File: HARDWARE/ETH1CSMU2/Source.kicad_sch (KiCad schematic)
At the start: 99 parts, among them Q901 FDV301N, U901 DAC8565ICPW, U902 AD9834BRUZ, U903 MC74AC161DR2G, U904 MAX6102EUR, U905 MAX5217GUA+, U906 SN74AHC1G14DBVT, U907 OPA2141AID, U908 MC74AC161DR2G, U909 SN74AUP1G79DCKR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

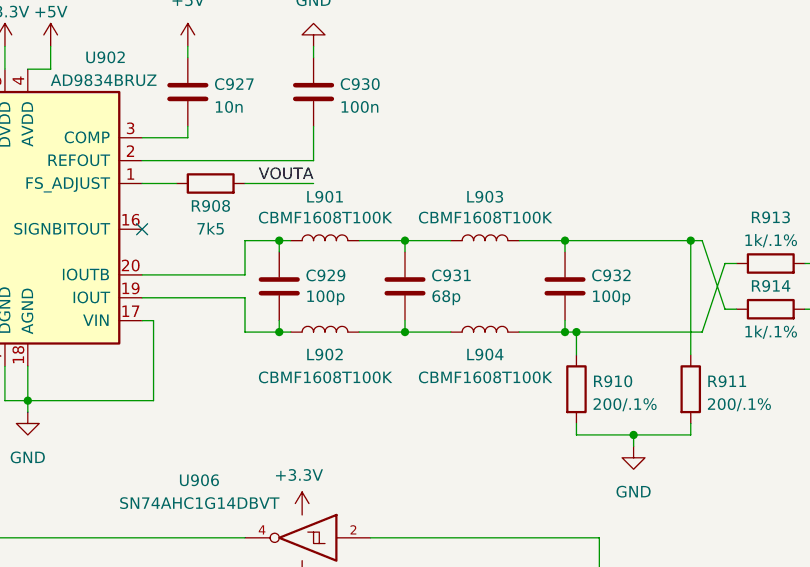
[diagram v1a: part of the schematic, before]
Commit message: Converter HW to KiCAD 7.0. Fixed 3D model paths.
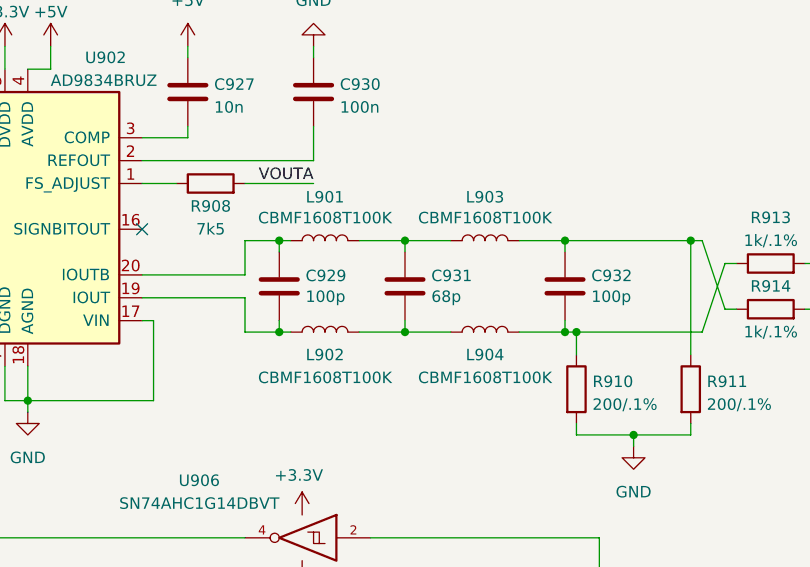
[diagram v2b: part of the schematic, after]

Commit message: Software development
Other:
- note added: "-25mV - +25mV"
- note added: "0 - 2V5"
- note added: "2V5"
- moved on the sheet: U904
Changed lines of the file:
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@@
   (junction (at 133.35 262.89) (diameter 0) (color 0 0 0 0)
   )
+  (junction (at 182.88 31.75) (diameter 0) (color 0 0 0 0)
+  )
   (junction (at 114.3 189.23) (diameter 0) (color 0 0 0 0)
   )
@@
   (junction (at 209.55 133.35) (diameter 0) (color 0 0 0 0)
   )
-  (junction (at 182.88 31.75) (diameter 0) (color 0 0 0 0)
-  )
   (junction (at 281.94 138.43) (diameter 0) (color 0 0 0 0)
   )
@@
     (stroke (width 0) (type default))
   )
+  (wire (pts (xy 182.88 31.75) (xy 182.88 53.34))
+    (stroke (width 0) (type default))
+  )
   (wire (pts (xy 34.29 262.89) (xy 40.64 262.89))
     (stroke (width 0) (type default))
@@
     (stroke (width 0) (type default))
   )
-  (wire (pts (xy 275.59 36.83) (xy 280.67 36.83))
+  (wire (pts (xy 275.59 36.83) (xy 294.64 36.83))
     (stroke (width 0) (type default))
   )
@@
     (stroke (width 0) (type default))
   )
-  (wire (pts (xy 182.88 31.75) (xy 182.88 53.34))
-    (stroke (width 0) (type default))
-  )
   (wire (pts (xy 246.38 44.45) (xy 246.38 45.72))
     (stroke (width 0) (type default))
@@
     (stroke (width 0) (type default))
   )
-  (wire (pts (xy 176.53 31.75) (xy 182.88 31.75))
+  (wire (pts (xy 152.4 31.75) (xy 182.88 31.75))
     (stroke (width 0) (type default))
   )
@@
     (effects (font (size 1.27 1.27)) (justify left bottom))
   )
+  (text "0 - 2V5" (at 196.85 62.23 0)
+    (effects (font (size 1.27 1.27)) (justify left bottom))
+  )
   (text "OFFSET DAC" (at 125.73 16.51 0)
     (effects (font (size 1.27 1.27)) (justify left bottom))
   )
+  (text "-25mV - +25mV" (at 276.86 35.56 0)
+    (effects (font (size 1.27 1.27)) (justify left bottom))
+  )
+  (text "2V5" (at 166.37 30.48 0)
+    (effects (font (size 1.27 1.27)) (justify left bottom))
+  )
   (text "DAC" (at 13.97 16.51 0)
     (effects (font (size 1.27 1.27)) (justify left bottom))
@@
     (effects (font (size 1.27 1.27)) (justify right))
   )
-  (hierarchical_label "VOUT_OFFSET" (shape output) (at 280.67 36.83 0) (fields_autoplaced)
+  (hierarchical_label "VOUT_OFFSET" (shape output) (at 294.64 36.83 0) (fields_autoplaced)
     (effects (font (size 1.27 1.27)) (justify left))
   )
@@
     )
   )
-  (symbol (lib_id "power:GND") (at 166.37 39.37 0) (unit 1)
+  (symbol (lib_id "power:GND") (at 142.24 39.37 0) (unit 1)
     (in_bom yes) (on_board yes) (dnp no) (fields_autoplaced)
-    (property "Reference" "#PWR0931" (at 166.37 45.72 0)
+    (property "Reference" "#PWR0931" (at 142.24 45.72 0)
       (effects (font (size 1.27 1.27)) hide)
     )
-    (property "Value" "GND" (at 166.37 43.8134 0)
+    (property "Value" "GND" (at 142.24 43.8134 0)
       (effects (font (size 1.27 1.27)))
     )
-    (property "Footprint" "" (at 166.37 39.37 0)
+    (property "Footprint" "" (at 142.24 39.37 0)
       (effects (font (size 1.27 1.27)) hide)
     )
-    (property "Datasheet" "" (at 166.37 39.37 0)
+    (property "Datasheet" "" (at 142.24 39.37 0)
       (effects (font (size 1.27 1.27)) hide)
     )
@@
     )
   )
-  (symbol (lib_id "power:+5V") (at 166.37 24.13 0) (unit 1)
+  (symbol (lib_id "power:+5V") (at 142.24 24.13 0) (unit 1)
     (in_bom yes) (on_board yes) (dnp no) (fields_autoplaced)
-    (property "Reference" "#PWR0930" (at 166.37 27.94 0)
+    (property "Reference" "#PWR0930" (at 142.24 27.94 0)
       (effects (font (size 1.27 1.27)) hide)
     )
-    (property "Value" "+5V" (at 166.37 20.5542 0)
+    (property "Value" "+5V" (at 142.24 20.5542 0)
       (effects (font (size 1.27 1.27)))
     )
-    (property "Footprint" "" (at 166.37 24.13 0)
+    (property "Footprint" "" (at 142.24 24.13 0)
       (effects (font (size 1.27 1.27)) hide)
     )
-    (property "Datasheet" "" (at 166.37 24.13 0)
+    (property "Datasheet" "" (at 142.24 24.13 0)
       (effects (font (size 1.27 1.27)) hide)
     )
@@
     )
   )
-  (symbol (lib_id "Reference_Voltage:MAX6102") (at 168.91 31.75 0) (unit 1)
+  (symbol (lib_id "Reference_Voltage:MAX6102") (at 144.78 31.75 0) (unit 1)
     (in_bom yes) (on_board yes) (dnp no) (fields_autoplaced)
-    (property "Reference" "U904" (at 163.0681 30.9153 0)
+    (property "Reference" "U904" (at 138.9381 30.9153 0)
       (effects (font (size 1.27 1.27)) (justify right))
     )
-    (property "Value" "MAX6102EUR" (at 163.0681 33.4522 0)
+    (property "Value" "MAX6102EUR" (at 138.9381 33.4522 0)
       (effects (font (size 1.27 1.27)) (justify right))
     )
-    (property "Footprint" "Package_TO_SOT_SMD:SOT-23" (at 171.45 39.37 0)
+    (property "Footprint" "Package_TO_SOT_SMD:SOT-23" (at 147.32 39.37 0)
       (effects (font (size 1.27 1.27) italic) hide)
     )
-    (property "Datasheet" "http://datasheets.maximintegrated.com/en/ds/MAX6100-MAX6107.pdf" (at 171.45 40.64 0)
+    (property "Datasheet" "http://datasheets.maximintegrated.com/en/ds/MAX6100-MAX6107.pdf" (at 147.32 40.64 0)
       (effects (font (size 1.27 1.27) italic) hide)
     )

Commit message: Software development
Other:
- note added: "-12V - +12V"
- note added: "0 - 1.25V"
- moved on the sheet: C937, R931, R932, R933, R937, U913, U915

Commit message: Software development and hardware changes.
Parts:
- R901: now not fitted
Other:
- note added: "0-2.5 V"
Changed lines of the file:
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@@
     (stroke (width 0) (type default))
   )
-  (wire (pts (xy 87.63 31.75) (xy 92.71 31.75))
+  (wire (pts (xy 87.63 31.75) (xy 104.14 31.75))
     (stroke (width 0) (type default))
   )
@@
     (stroke (width 0) (type default))
   )
-  (wire (pts (xy 87.63 34.29) (xy 92.71 34.29))
+  (wire (pts (xy 87.63 34.29) (xy 104.14 34.29))
     (stroke (width 0) (type default))
   )
@@
     (stroke (width 0) (type default))
   )
-  (wire (pts (xy 87.63 39.37) (xy 92.71 39.37))
+  (wire (pts (xy 87.63 39.37) (xy 104.14 39.37))
     (stroke (width 0) (type default))
   )
@@
     (stroke (width 0) (type default))
   )
-  (wire (pts (xy 87.63 36.83) (xy 92.71 36.83))
+  (wire (pts (xy 87.63 36.83) (xy 104.14 36.83))
     (stroke (width 0) (type default))
   )
@@
   (wire (pts (xy 15.24 241.3) (xy 15.24 240.03))
     (stroke (width 0) (type default))
+  )
+  (text_box "Externeal reference must be 4V - 4.99V. The 2.5V is to small. Best solution is to use REF5040ID. DAC1_LDAC is not needed (connect to GND)."
+    (at 43.18 77.47 0) (size 58.42 7.62)
+    (stroke (width 0) (type default))
+    (fill (type none))
+    (effects (font (size 1.27 1.27)) (justify left top))
   )
   (text "0 - 1.25V" (at 337.82 181.61 0)
@@
     (effects (font (size 1.27 1.27)) (justify left bottom))
   )
+  (text "0-2.5 V" (at 92.71 29.21 0)
+    (effects (font (size 1.27 1.27)) (justify left bottom))
+  )
   (text "OFFSET DAC" (at 125.73 16.51 0)
     (effects (font (size 1.27 1.27)) (justify left bottom))
@@
     (effects (font (size 1.27 1.27)) (justify left))
   )
-  (hierarchical_label "VC_-IN" (shape output) (at 92.71 34.29 0) (fields_autoplaced)
+  (hierarchical_label "VC_-IN" (shape output) (at 104.14 34.29 0) (fields_autoplaced)
     (effects (font (size 1.27 1.27)) (justify left))
   )
@@
     (effects (font (size 1.27 1.27)) (justify right))
   )
-  (hierarchical_label "VC_SRC" (shape output) (at 92.71 39.37 0) (fields_autoplaced)
+  (hierarchical_label "VC_SRC" (shape output) (at 104.14 39.37 0) (fields_autoplaced)
     (effects (font (size 1.27 1.27)) (justify left))
   )
@@
     (effects (font (size 1.27 1.27)) (justify right))
   )
-  (hierarchical_label "VC_+IN" (shape output) (at 92.71 31.75 0) (fields_autoplaced)
+  (hierarchical_label "VC_+IN" (shape output) (at 104.14 31.75 0) (fields_autoplaced)
     (effects (font (size 1.27 1.27)) (justify left))
   )
@@
     (effects (font (size 1.27 1.27)) (justify right))
   )
-  (hierarchical_label "VC_SINK" (shape output) (at 92.71 36.83 0) (fields_autoplaced)
+  (hierarchical_label "VC_SINK" (shape output) (at 104.14 36.83 0) (fields_autoplaced)
     (effects (font (size 1.27 1.27)) (justify left))
   )
@@
   )
   (symbol (lib_id "Device:R") (at 22.86 66.04 0) (unit 1)
-    (in_bom yes) (on_board yes) (dnp no) (fields_autoplaced)
+    (in_bom yes) (on_board yes) (dnp yes) (fields_autoplaced)
     (property "Reference" "R901" (at 25.4 64.7699 0)
       (effects (font (size 1.27 1.27)) (justify left))

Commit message: Software development, added comments to schematic.
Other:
- note added: "gain 3x"
- moved on the sheet: C921, C927, C929, C930, C931, C932, C933, C934, C935, C937, C938, L901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

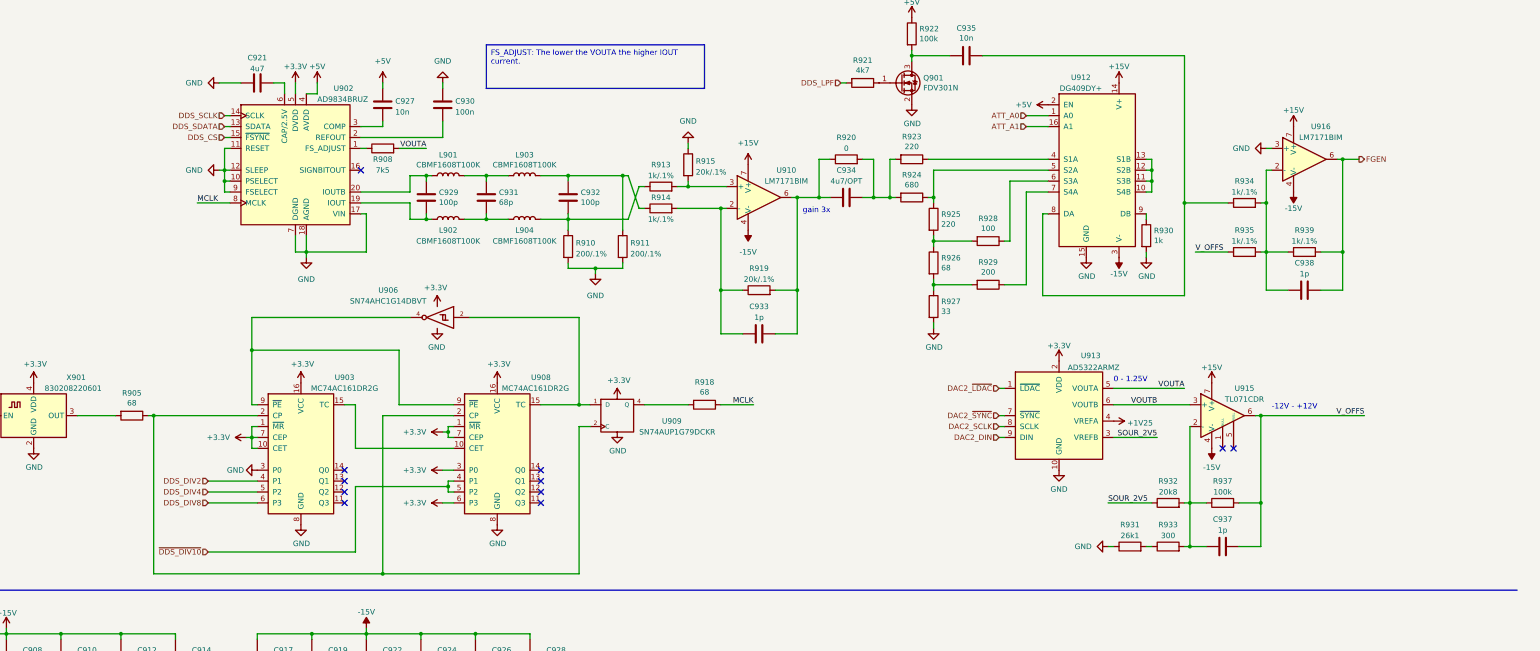
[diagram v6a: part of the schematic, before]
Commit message: Software development and hardware changes. FGEN code works.
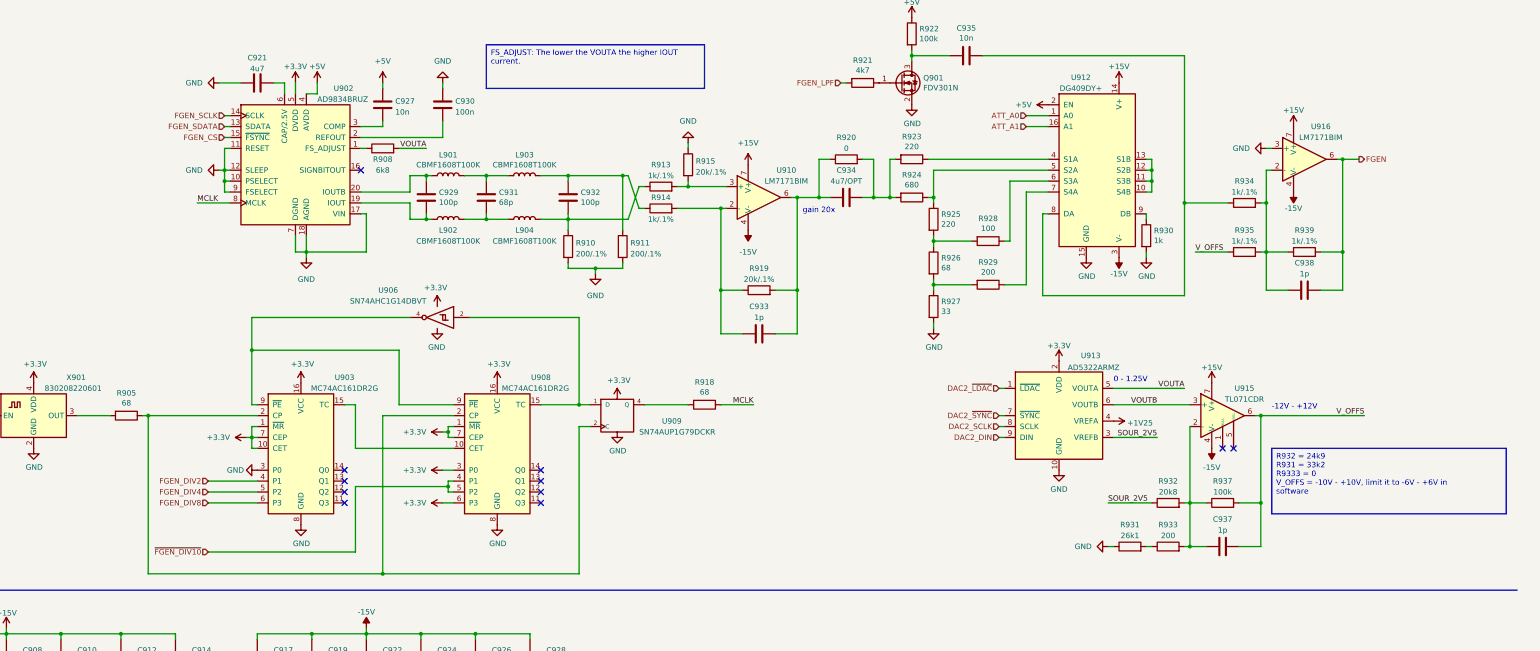
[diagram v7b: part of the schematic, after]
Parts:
- R908: value 7k5 -> 6k8
- R933: value 300 -> 200
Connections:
- net DDS_CS renamed FGEN_CS
- net DDS_DIV2 renamed FGEN_DIV2
- net DDS_DIV4 renamed FGEN_DIV4
- net DDS_DIV8 renamed FGEN_DIV8
- net DDS_LPF renamed FGEN_LPF
- net DDS_SCLK renamed FGEN_SCLK
- net DDS_SDATA renamed FGEN_SDATA
- net ~{DDS_DIV10} renamed ~{FGEN_DIV10}
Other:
- note added: "gain 20x"
- note removed: "gain 3x"
- moved on the sheet: R905
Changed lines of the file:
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@@
   (junction (at 182.88 31.75) (diameter 0) (color 0 0 0 0)
   )
-  (junction (at 88.9 189.23) (diameter 0) (color 0 0 0 0)
-  )
   (junction (at 35.56 44.45) (diameter 0) (color 0 0 0 0)
   )
@@
   (junction (at 260.35 138.43) (diameter 0) (color 0 0 0 0)
   )
+  (junction (at 87.63 189.23) (diameter 0) (color 0 0 0 0)
+  )
   (junction (at 111.76 173.99) (diameter 0) (color 0 0 0 0)
   )
@@
     (stroke (width 0) (type default))
   )
-  (wire (pts (xy 113.03 189.23) (xy 88.9 189.23))
+  (wire (pts (xy 87.63 189.23) (xy 113.03 189.23))
     (stroke (width 0) (type default))
   )
@@
     (stroke (width 0) (type default))
   )
-  (wire (pts (xy 88.9 226.06) (xy 88.9 189.23))
+  (wire (pts (xy 87.63 226.06) (xy 87.63 189.23))
     (stroke (width 0) (type default))
   )
@@
     (stroke (width 0) (type default))
   )
-  (wire (pts (xy 80.01 189.23) (xy 71.12 189.23))
+  (wire (pts (xy 78.74 189.23) (xy 71.12 189.23))
     (stroke (width 0) (type default))
   )
@@
     (stroke (width 0) (type default))
   )
+  (wire (pts (xy 87.63 189.23) (xy 86.36 189.23))
+    (stroke (width 0) (type default))
+  )
   (wire (pts (xy 270.51 160.02) (xy 270.51 158.75))
     (stroke (width 0) (type default))
@@
     (stroke (width 0) (type default))
   )
-  (wire (pts (xy 142.24 226.06) (xy 88.9 226.06))
+  (wire (pts (xy 142.24 226.06) (xy 87.63 226.06))
     (stroke (width 0) (type default))
   )
@@
     (stroke (width 0) (type default))
   )
-  (wire (pts (xy 88.9 189.23) (xy 87.63 189.23))
-    (stroke (width 0) (type default))
-  )
   (wire (pts (xy 297.18 129.54) (xy 269.24 129.54))
     (stroke (width 0) (type default))
@@
     (effects (font (size 1.27 1.27)) (justify left top))
   )
+  (text_box "R932 = 24k9\nR931 = 33k2\nR9333 = 0\nV_OFFS = -10V - +10V, limit it to -6V - +6V in software\n"
+    (at 349.25 196.85 0) (size 54.61 15.24)
+    (stroke (width 0) (type default))
+    (fill (type none))
+    (effects (font (size 1.27 1.27)) (justify left top))
+  )
   (text_box "FS_ADJUST: The lower the VOUTA the higher IOUT current. "
     (at 166.37 102.87 0) (size 50.8 10.16)
@@
     (effects (font (size 1.27 1.27)) (justify left bottom))
   )
-  (text "gain 3x" (at 240.03 142.24 0)
+  (text "gain 20x" (at 240.03 142.24 0)
     (effects (font (size 1.27 1.27)) (justify left bottom))
   )
@@
     (effects (font (size 1.27 1.27)) (justify right bottom))
   )
-  (hierarchical_label "DDS_DIV4" (shape input) (at 101.6 207.01 180) (fields_autoplaced)
+  (hierarchical_label "FGEN_DIV4" (shape input) (at 101.6 207.01 180) (fields_autoplaced)
     (effects (font (size 1.27 1.27)) (justify right))
   )
@@
     (effects (font (size 1.27 1.27)) (justify left))
   )
-  (hierarchical_label "DDS_DIV2" (shape input) (at 101.6 204.47 180) (fields_autoplaced)
+  (hierarchical_label "FGEN_DIV2" (shape input) (at 101.6 204.47 180) (fields_autoplaced)
     (effects (font (size 1.27 1.27)) (justify right))
   )
-  (hierarchical_label "DDS_SCLK" (shape input) (at 105.41 119.38 180) (fields_autoplaced)
+  (hierarchical_label "FGEN_SCLK" (shape input) (at 105.41 119.38 180) (fields_autoplaced)
     (effects (font (size 1.27 1.27)) (justify right))
   )
@@
     (effects (font (size 1.27 1.27)) (justify right))
   )
-  (hierarchical_label "~{DDS_DIV10}" (shape input) (at 101.6 220.98 180) (fields_autoplaced)
+  (hierarchical_label "~{FGEN_DIV10}" (shape input) (at 101.6 220.98 180) (fields_autoplaced)
     (effects (font (size 1.27 1.27)) (justify right))
   )
-  (hierarchical_label "DDS_DIV8" (shape input) (at 101.6 209.55 180) (fields_autoplaced)
+  (hierarchical_label "FGEN_DIV8" (shape input) (at 101.6 209.55 180) (fields_autoplaced)
     (effects (font (size 1.27 1.27)) (justify right))
   )
@@
     (effects (font (size 1.27 1.27)) (justify left))
   )
-  (hierarchical_label "DDS_CS" (shape input) (at 105.41 124.46 180) (fields_autoplaced)
+  (hierarchical_label "FGEN_CS" (shape input) (at 105.41 124.46 180) (fields_autoplaced)
     (effects (font (size 1.27 1.27)) (justify right))
   )
@@
     (effects (font (size 1.27 1.27)) (justify right))
   )
-  (hierarchical_label "DDS_LPF" (shape input) (at 248.92 111.76 180) (fields_autoplaced)
+  (hierarchical_label "FGEN_LPF" (shape input) (at 248.92 111.76 180) (fields_autoplaced)
     (effects (font (size 1.27 1.27)) (justify right))
   )
@@
     (effects (font (size 1.27 1.27)) (justify left))
   )
-  (hierarchical_label "DDS_SDATA" (shape input) (at 105.41 121.92 180) (fields_autoplaced)
+  (hierarchical_label "FGEN_SDATA" (shape input) (at 105.41 121.92 180) (fields_autoplaced)
     (effects (font (size 1.27 1.27)) (justify right))
   )
@@
       (effects (font (size 1.27 1.27)))
     )
-    (property "Value" "300" (at 325.12 217.17 90)
+    (property "Value" "200" (at 325.12 217.17 90)
       (effects (font (size 1.27 1.27)))
     )
@@
       (effects (font (size 1.27 1.27)))
     )
-    (property "Value" "7k5" (at 142.24 132.08 90)
+    (property "Value" "6k8" (at 142.24 132.08 90)
       (effects (font (size 1.27 1.27)))
     )
@@
     )
   )
-  (symbol (lib_id "Device:R") (at 83.82 189.23 270) (unit 1)
+  (symbol (lib_id "Device:R") (at 82.55 189.23 270) (unit 1)
     (in_bom yes) (on_board yes) (dnp no)
-    (property "Reference" "R905" (at 83.82 183.9722 90)
+    (property "Reference" "R905" (at 82.55 183.9722 90)
       (effects (font (size 1.27 1.27)))
     )
-    (property "Value" "68" (at 83.82 186.2836 90)
+    (property "Value" "68" (at 82.55 186.2836 90)
       (effects (font (size 1.27 1.27)))
     )
-    (property "Footprint" "Resistor_SMD:R_0603_1608Metric_Pad0.98x0.95mm_HandSolder" (at 83.82 187.452 90)
+    (property "Footprint" "Resistor_SMD:R_0603_1608Metric_Pad0.98x0.95mm_HandSolder" (at 82.55 187.452 90)
       (effects (font (size 1.27 1.27)) hide)
     )
-    (property "Datasheet" "~" (at 83.82 189.23 0)
+    (property "Datasheet" "~" (at 82.55 189.23 0)
       (effects (font (size 1.27 1.27)) hide)
     )

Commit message: Development
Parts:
- C934: value 4u7/OPT -> 4u7
- R920: now not fitted
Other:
- note added: "VREF"
- note added: "gain 8x"
- note removed: "0-2.5 V"
- note removed: "gain 20x"
- moved on the sheet: C921, C927, C929, C930, C931, C932, C933, C934, C935, C937, C938, L901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
